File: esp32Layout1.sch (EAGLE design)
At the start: 37 parts, among them U1 ESP-WROOM-32, Y3 32.768kHz

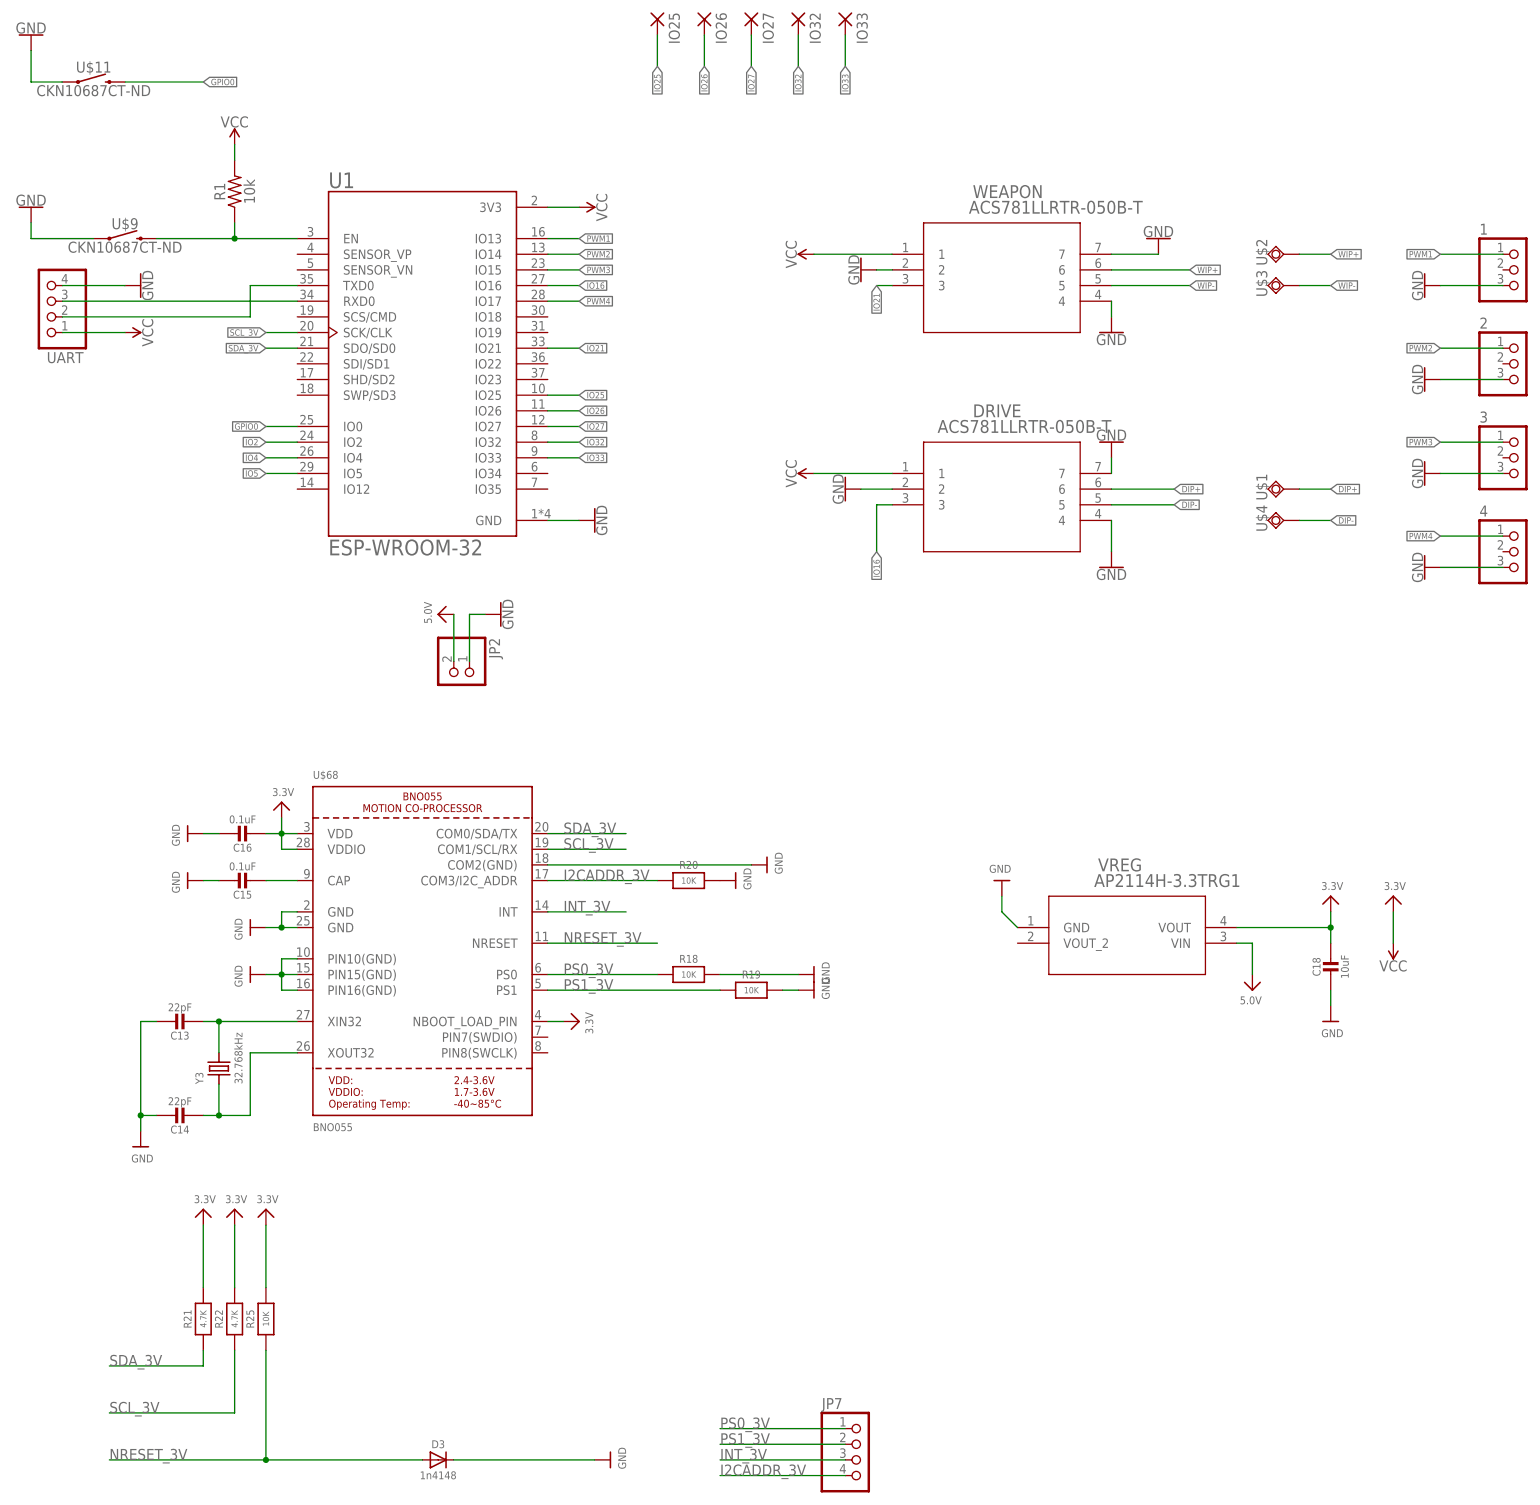
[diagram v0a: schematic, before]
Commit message: 2nd bno055 version, sent to JLC for production
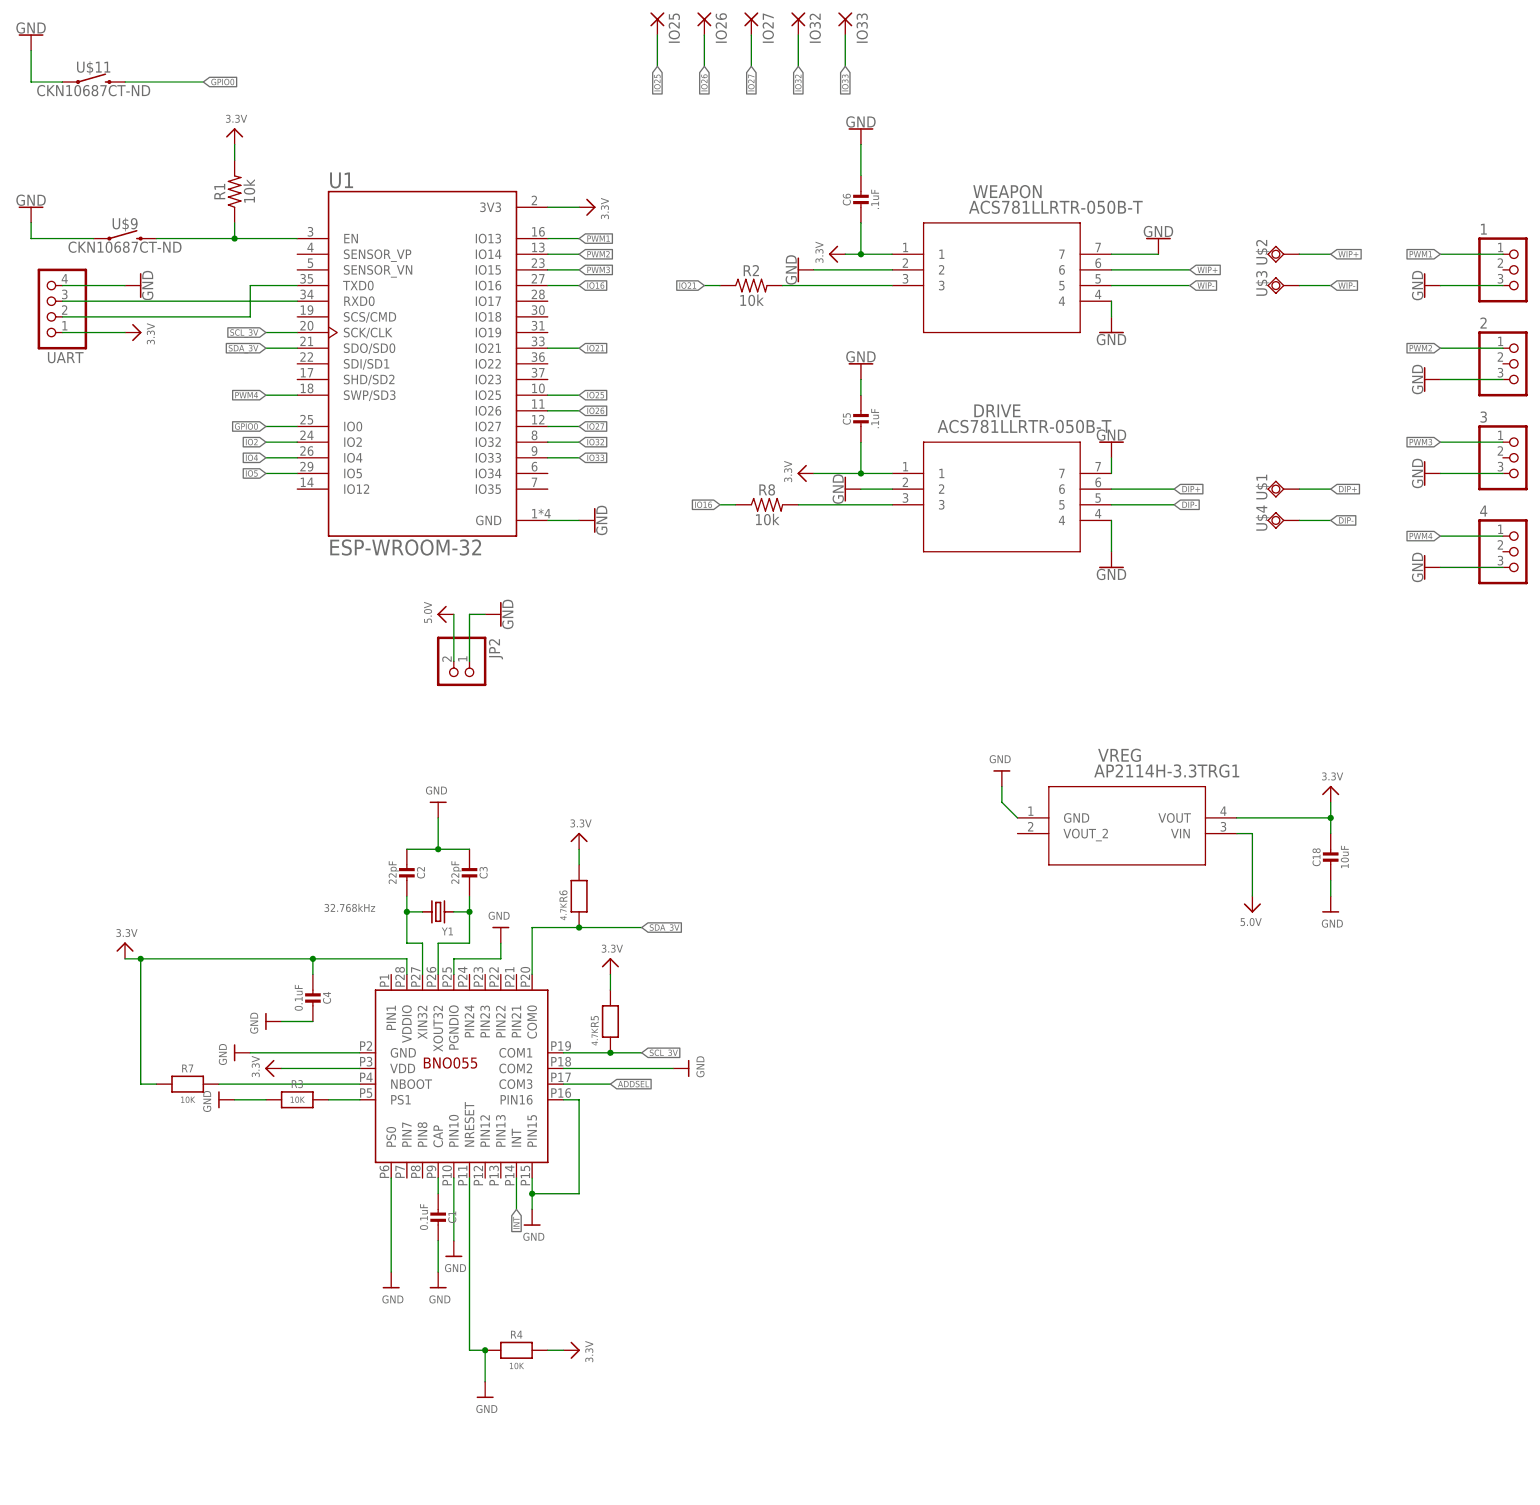
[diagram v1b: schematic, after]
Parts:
- removed C13, C14: 22pF, microbuilder:CAP_CERAMIC0805-NOOUTLINE
- removed C15: 0.1uF, microbuilder:CAP_CERAMIC0805-NOOUTLINE
- removed C16: 0.1uF, microbuilder:CAP_CERAMIC0805_10MGAP
- removed D3: 1n4148, microbuilder:DIODESOD-323
- removed JP7: (no value), microbuilder:HEADER-1X476MIL
- removed R18, R19, R20, R25: 10K, microbuilder:RESISTOR0805_NOOUTLINE
- removed R21, R22: 4.7K, microbuilder:RESISTOR0805_NOOUTLINE
- removed U$68: BNO055, microbuilder:BNO055
- removed Y3: 32.768kHz, microbuilder:CRYSTAL8.0X3.8
- added BNO055: BNO055, Tim Parts:BNO055
- added C1, C4: 0.1uF, microbuilder:CAP_CERAMIC0805-NOOUTLINE
- added C2, C3: 22pF, microbuilder:CAP_CERAMIC0805-NOOUTLINE
- added C5, C6: .1uF, microbuilder:CAP_CERAMIC0805_10MGAP
- added R2, R8: 10k, SparkFun-Resistors:10KOHM-0603-1/10W-1%
- added R3, R4, R7: 10K, microbuilder:RESISTOR0805_NOOUTLINE
- added R5, R6: 4.7K, microbuilder:RESISTOR0805_NOOUTLINE
- added Y1: 32.768kHz, microbuilder:CRYSTAL8.0X3.8
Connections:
- removed net I2CADDR_3V: JP7.4, R20.1, U$68.COM3/I2C_ADDR
- removed net INT_3V: JP7.3, U$68.INT
- removed net NRESET_3V: D3.A, R25.1, U$68.NRESET
- removed net PS0_3V: JP7.1, R18.1, U$68.PS0
- removed net PS1_3V: JP7.2, R19.1, U$68.PS1
- removed net VCC: DRIVE.1, R1.2, U1.3V3, UART.1, WEAPON.1
- new net ADDSEL: BNO055.COM3
- new net INT: BNO055.INT
- new net N$1: BNO055.PS1, R3.2
- new net N$5: R2.2, WEAPON.3
- new net N$6: BNO055.CAP, C1.2
- new net N$7: BNO055.XIN32, C2.1, Y1.2
- new net N$8: BNO055.XOUT32, C3.1, Y1.1
- new net N$9: BNO055.NBOOT, R7.2
- net 3.3V: now also BNO055.VDD, BNO055.VDDIO, C4.2, R1.2, R4.2, R5.2, R6.2, R7.1, U1.3V3, UART.1; no longer C16.2, R21.2, R22.2, R25.2, U$68.NBOOT_LOAD_PIN, U$68.VDD, U$68.VDDIO
- net GND: now also BNO055.COM2, BNO055.GND, BNO055.NRESET, BNO055.PGNDIO, BNO055.PIN10, BNO055.PIN15, BNO055.PIN16, BNO055.PS0, C1.1, C2.2, C3.2, C4.1, C5.1, C6.1, R3.1, R4.1; no longer C13.1, C14.1, C15.1, C16.1, D3.C, R18.2, R19.2, R20.2, U$68.COM2(GND), U$68.GND@1, U$68.GND@2, U$68.PIN10(GND), U$68.PIN15(GND), U$68.PIN16(GND)
- net IO16: now also R8.1; no longer DRIVE.3
- net IO21: now also R2.1; no longer WEAPON.3
- net N$10: now also DRIVE.3, R8.2; no longer C13.2, U$68.XIN32, Y3.2
- net N$11: now also C5.2, DRIVE.1; no longer C14.2, U$68.XOUT32, Y3.1
- net N$12: now also C6.2, WEAPON.1; no longer C15.2, U$68.CAP
- net PWM4: now also U1.SWP/SD3; no longer U1.IO17
- net SCL_3V: now also BNO055.COM1, R5.1; no longer R22.1, U$68.COM1/SCL/RX
- net SDA_3V: now also BNO055.COM0, R6.1; no longer R21.1, U$68.COM0/SDA/TX
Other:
- moved on the sheet: C18, VREG

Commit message: Version 2.1 offical OSH PARK release
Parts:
- added AD, NR, SCL, SDA: (no value), wirepad:SMD2
- added C7: 10 uF, microbuilder:CAP_CERAMIC0805-NOOUTLINE
- added R9: 4.7K, microbuilder:RESISTOR0805_NOOUTLINE
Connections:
- removed net IO16: R8.1, U1.IO16
- removed net IO21: R2.1, U1.IO21
- removed net N$11: C5.2, DRIVE.1
- removed net N$12: C6.2, WEAPON.1
- new net IO34: R2.1, U1.IO34
- new net IO35: R8.1, U1.IO35
- new net NRESET: BNO055.NRESET, NR.P, R4.1
- net 3.3V: now also C5.2, C6.2, DRIVE.1, WEAPON.1
- net 5.0V: now also C7.2
- net ADDSEL: now also AD.P, R9.1
- net GND: now also C7.1, R9.2; no longer BNO055.NRESET, R4.1
- net PWM4: now also U1.IO19; no longer U1.SWP/SD3
- net SCL_3V: now also SCL.P, U1.IO22; no longer U1.SCK/CLK
- net SDA_3V: now also SDA.P, U1.IO21; no longer U1.SDO/SD0
